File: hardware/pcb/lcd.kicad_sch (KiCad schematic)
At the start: 10 parts, among them J500 AXT524124, U500 LT3491

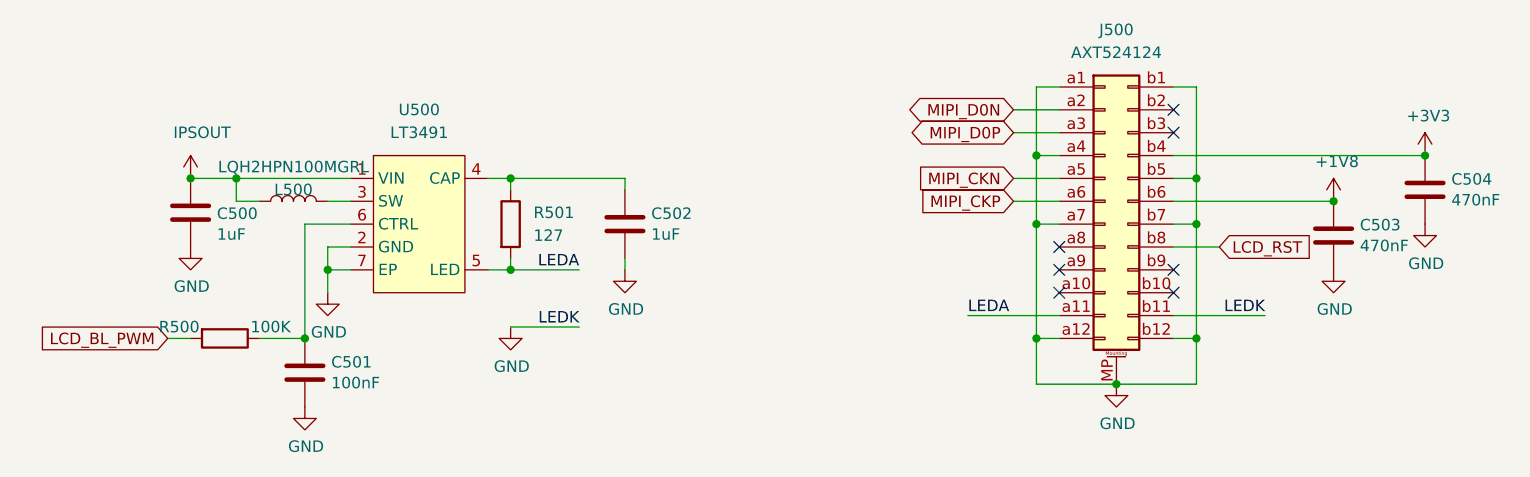
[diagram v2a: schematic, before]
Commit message: - pcb: r0p4, update to KiCAD 6.0
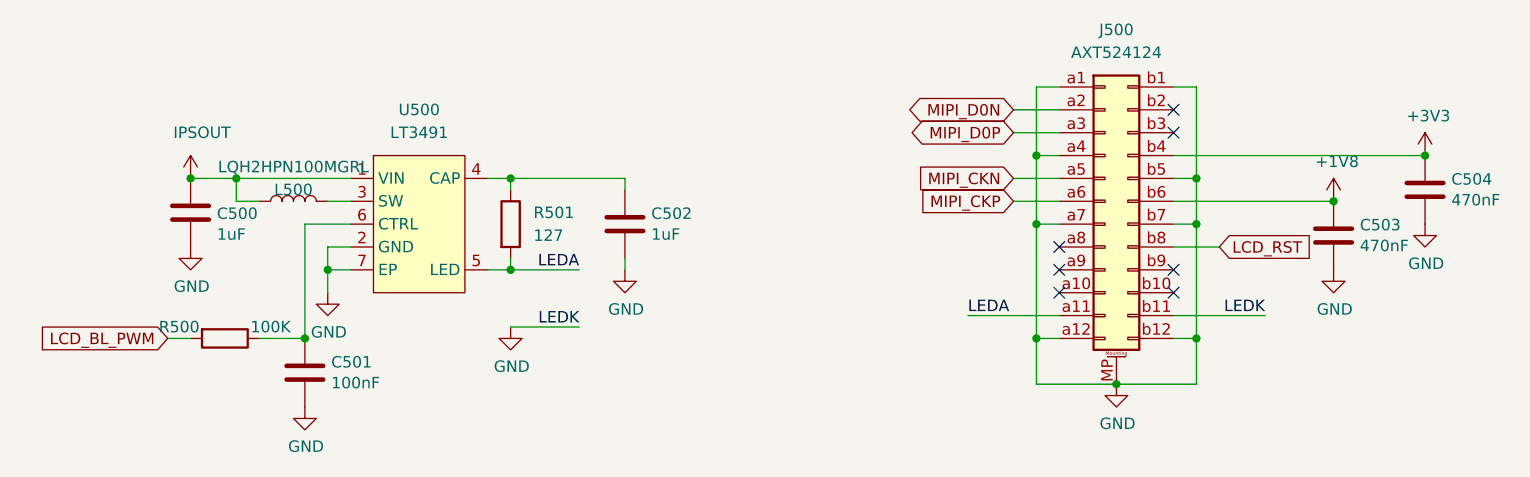
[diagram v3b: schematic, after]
